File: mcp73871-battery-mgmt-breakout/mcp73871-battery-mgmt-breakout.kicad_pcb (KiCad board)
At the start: 2 copper layers, 27.9 x 27.9 mm, 19 parts, among them J1 MICRO USB, J2 JST PH, J3 BREAKOUT1, J4 BREAKOUT2, U1 MCP73871

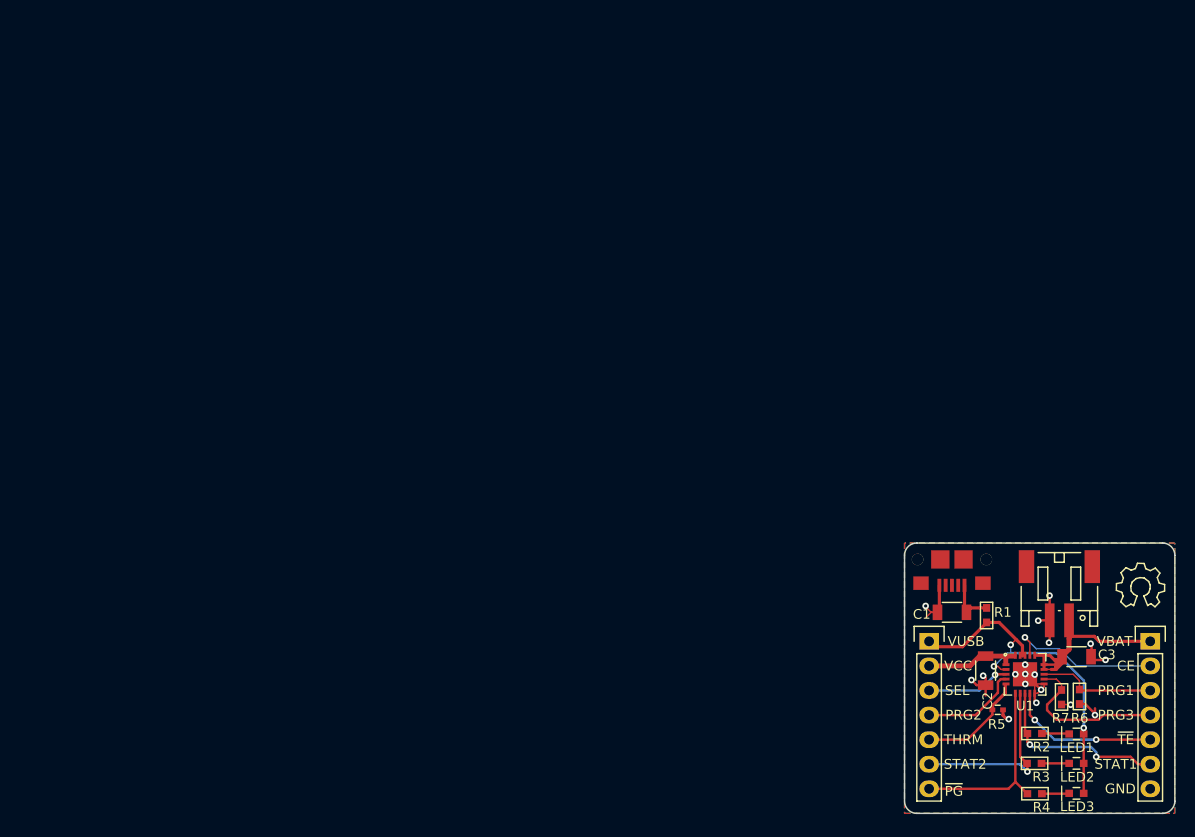
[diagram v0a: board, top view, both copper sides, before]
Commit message: Updating v1.0 with FabNotes file.
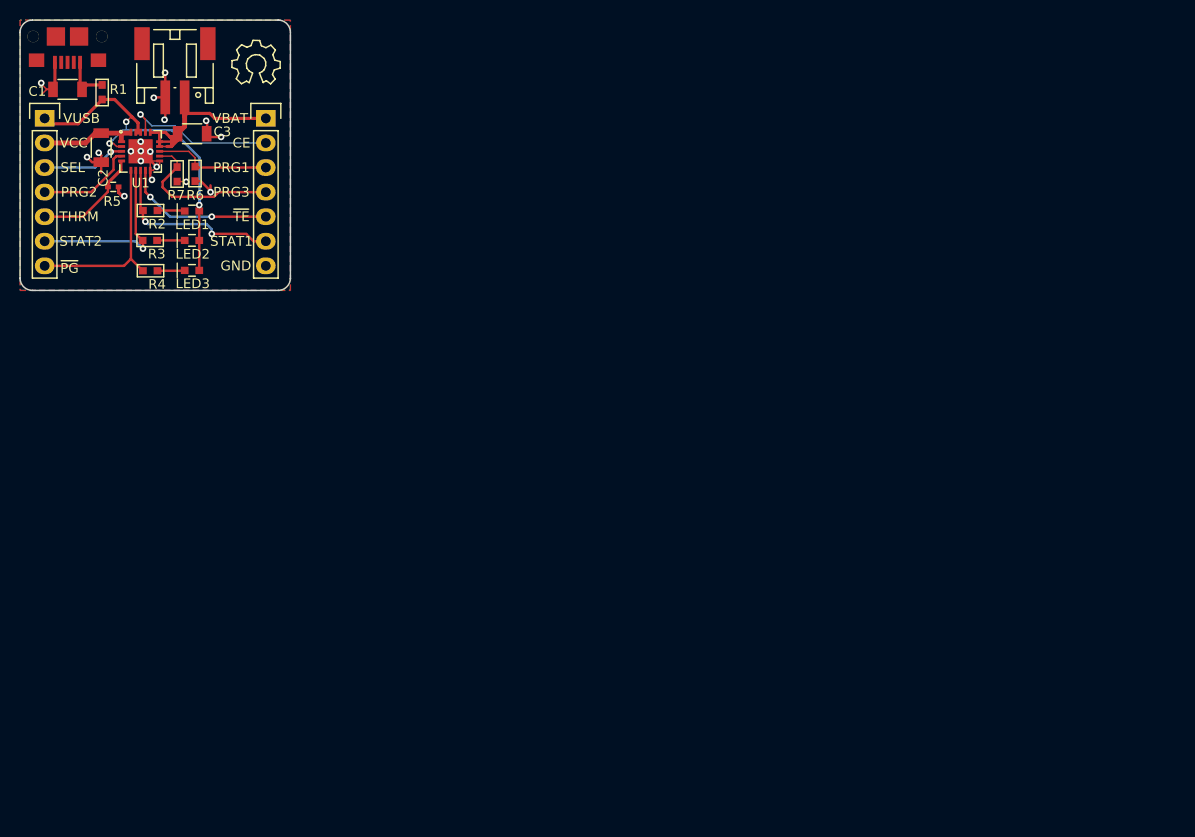
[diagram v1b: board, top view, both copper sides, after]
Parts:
- moved C2 106.2 mm to (31.3, 32.8)
- moved C3 106.2 mm to (40.7, 31.4)
- moved J2 106.2 mm to (38.9, 24.8)
- moved J3 106.2 mm to (25.4, 29.8)
- moved LED1 106.2 mm to (40.7, 39.3)
- moved LED2 106.2 mm to (40.7, 42.4)
- moved LED3 106.2 mm to (40.7, 45.5)
- moved R1 106.2 mm to (31.4, 27.1)
- moved R2 106.2 mm to (36.3, 39.3)
- moved R3 106.2 mm to (36.3, 42.4)
- moved R4 106.2 mm to (36.3, 45.5)
- moved R5 106.2 mm to (32.5, 36.8)
- moved R7 106.2 mm to (39.1, 35.5)
- moved REF** 106.2 mm to (47.3, 24.2)
- moved C1 106.2 mm to (27.8, 26.8)
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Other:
- board text added: "FABRICATION NOTES 1. THIS IS A 2 LAYER BOARD. 2. EXTERNAL LAYERS SHALL HAVE 1 OZ COPPER. 3. MATERIAL: FR4 AND 0.062 INCH +/- 10% THICK. 4. BOARDS SHALL BE ROHS COMPLIANT. 5. MANUFACTURE IN ACCORDANCE WITH IPC-6012 CLASS 2 6. MASK: BOTH SIDES OF THE BOARD SHALL HAVE SOLDER MASK (ANY COLOR) OVER BARE COPPER. 7. SILK: BOTH SIDES OF THE BOARD SHALL HAVE WHITE SILKSCREEN. DO NOT PLACE SILK OVER BARE C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"
